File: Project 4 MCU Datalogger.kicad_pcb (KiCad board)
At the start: 2 copper layers, 29 parts, among them J1 Conn_02x03_Odd_Even, J2 Conn_01x04_Pin, J3 Conn_01x09_Pin, J4 Conn_01x04_Pin, U1 24LC1025, U2 24LC1025, U3 DS1337S_, U4 ATMEGA328P-AU, Y1 32.768kHZ, Y2 16MHz

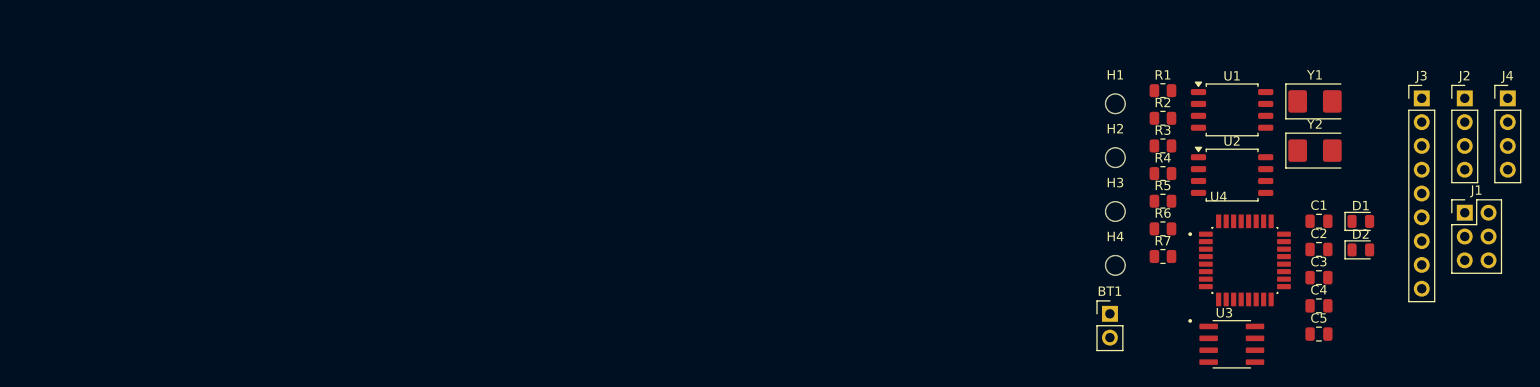
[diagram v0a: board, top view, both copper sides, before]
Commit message: Placed footprints on the Pcbnew.
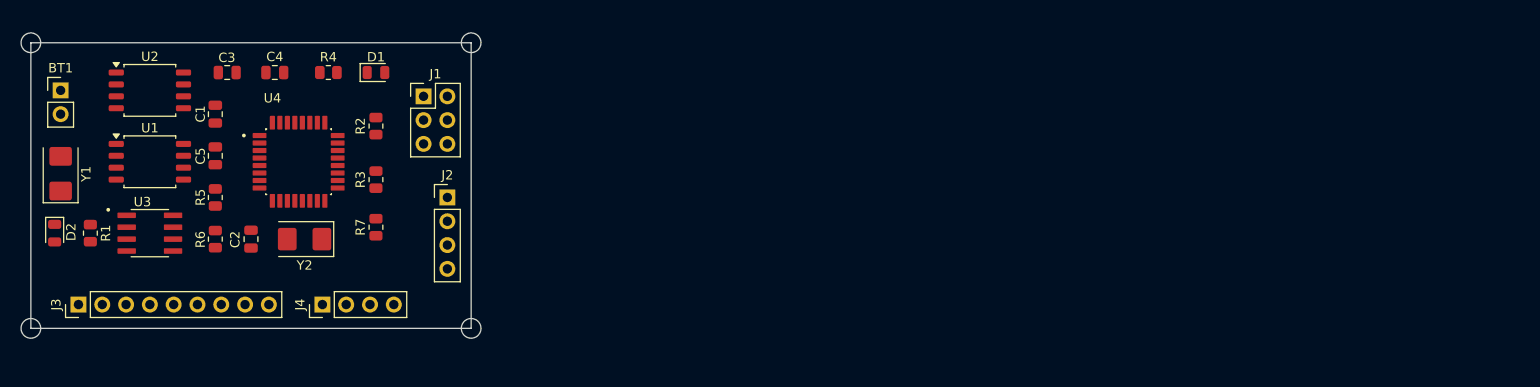
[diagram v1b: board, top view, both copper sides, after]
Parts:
- moved J3 145.0 mm to (106.7, 104.1), turned to 90 degrees
- moved D2 139.4 mm to (104.1, 96.5), turned to -90 degrees
- moved Y1 134.1 mm to (104.8, 90.2), turned to 90 degrees
- moved J4 128.4 mm to (132.7, 104.1), turned to 90 degrees
- moved C5 119.3 mm to (121.3, 88.3), turned to 90 degrees
- moved C3 118.6 mm to (122.6, 79.4), turned to 180 degrees
- moved C1 118.3 mm to (121.3, 83.8), turned to -90 degrees
- moved U3 116.1 mm to (114.3, 96.5)
- moved H4 115.9 mm to (101.6, 106.7)
- moved H1 115.9 mm to (101.6, 76.2)
- moved U2 115.9 mm to (114.3, 81.3)
- moved U1 115.6 mm to (114.3, 88.9)
- moved R1 115.5 mm to (108.0, 96.5), turned to -90 degrees
- moved BT1 114.5 mm to (104.8, 81.3)
- moved C4 114.2 mm to (127.6, 79.4)
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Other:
- board outline added: 47 x 30.5 mm

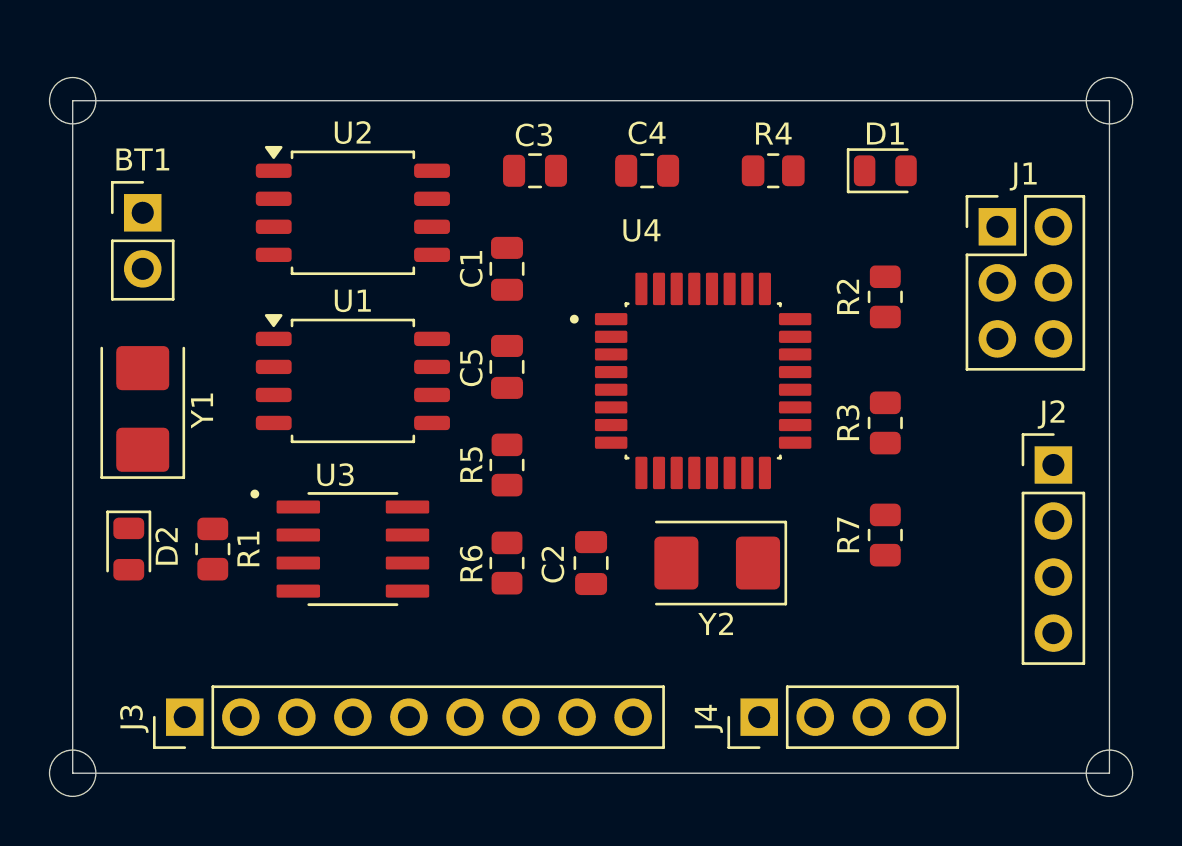
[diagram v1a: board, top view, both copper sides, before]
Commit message: Placed tracks on the Pcbnew.
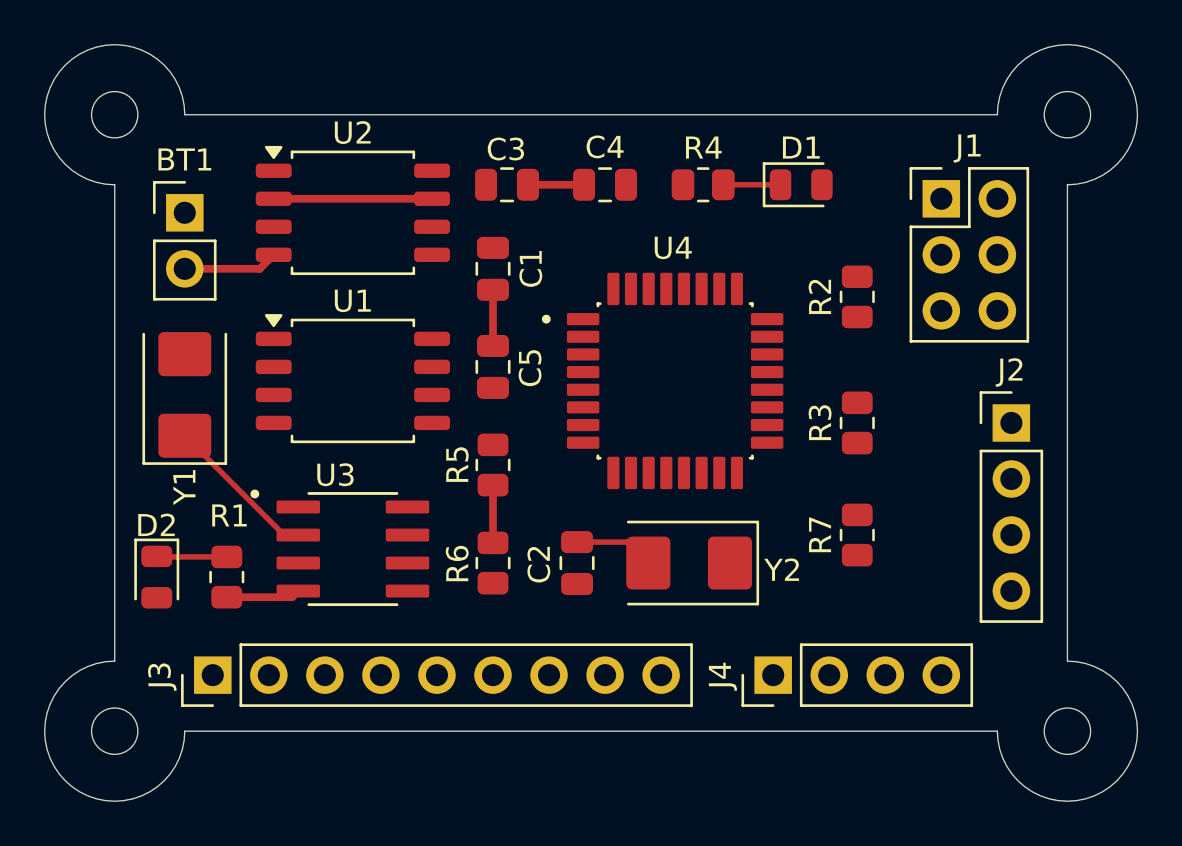
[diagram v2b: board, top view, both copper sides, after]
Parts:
- moved D1 3.86 mm to (134.6, 80.0)
- moved R4 3.24 mm to (130.2, 80.0)
- moved J1 2.84 mm to (141.0, 80.6)
- moved H3 2.69 mm to (146.7, 104.8)
- moved H4 2.69 mm to (103.5, 104.8)
- moved J2 2.69 mm to (144.1, 90.8)
- moved J3 2.29 mm to (108.0, 102.2)
- moved C4 2.01 mm to (125.7, 80.0)
- moved Y1 2.01 mm to (106.7, 89.5)
- moved H1 2.01 mm to (103.5, 76.8)
- moved H2 2.01 mm to (146.7, 76.8)
- moved J4 2.01 mm to (133.3, 102.2)
- moved BT1 1.91 mm to (106.7, 81.3)
- moved D2 1.80 mm to (105.4, 97.8)
- moved C3 1.42 mm to (121.3, 80.0)
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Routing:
- net GND: track 0.00 -> 19.9 mm
- net Net-(U3-X2): track 0.00 -> 7.01 mm
- net Net-(U4-PB6): track 0.00 -> 3.62 mm
- net Net-(D2-K): track 0.00 -> 3.19 mm
- net /Vcc: track 0.00 -> 2.62 mm
- net Net-(D1-K): track 0.00 -> 2.59 mm
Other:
- board size 47 x 30.5 mm -> 49.5 x 34.3 mm

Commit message: Wiring completed.
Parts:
- added REF**: KiCad-Logo2_5mm_SilkScreen, Symbol:KiCad-Logo2_5mm_SilkScreen, B.Cu at (114.3, 97.5)
- moved R2 5.72 mm to (137.2, 90.8)
- moved R3 5.72 mm to (137.2, 85.1)
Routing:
- net /Vcc: track 2.62 -> 142.4 mm, vias 0 -> 23
- net GND: track 19.9 -> 92.7 mm, vias 0 -> 8
- net /SCL: track 0.00 -> 60.7 mm, vias 0 -> 4
- net /SDA: track 0.00 -> 55.4 mm, vias 0 -> 3
- net /MOSI: track 0.00 -> 36.2 mm, vias 0 -> 2
- net /D2: track 0.00 -> 33.9 mm, vias 0 -> 2
- net /TX: track 0.00 -> 30.5 mm, vias 0 -> 2
- net /MISO: track 0.00 -> 28.4 mm, vias 0 -> 2
- net /D3: track 0.00 -> 27.9 mm, vias 0 -> 2
- net Net-(U4-PB7): track 0.00 -> 27.5 mm, vias 0 -> 2
- net /RESET: track 0.00 -> 26.0 mm, vias 0 -> 2
- net /D4: track 0.00 -> 24.6 mm, vias 0 -> 2
- net /RX: track 0.00 -> 22.0 mm, vias 0 -> 2
- net /SCK: track 0.00 -> 20.7 mm
- net Net-(U4-AREF): track 0.00 -> 18.2 mm
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- added copper zone on F.Cu, net /Vcc
- added copper zone on B.Cu, net GND
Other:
- board size 49.5 x 34.3 mm -> 48.5 x 33.3 mm

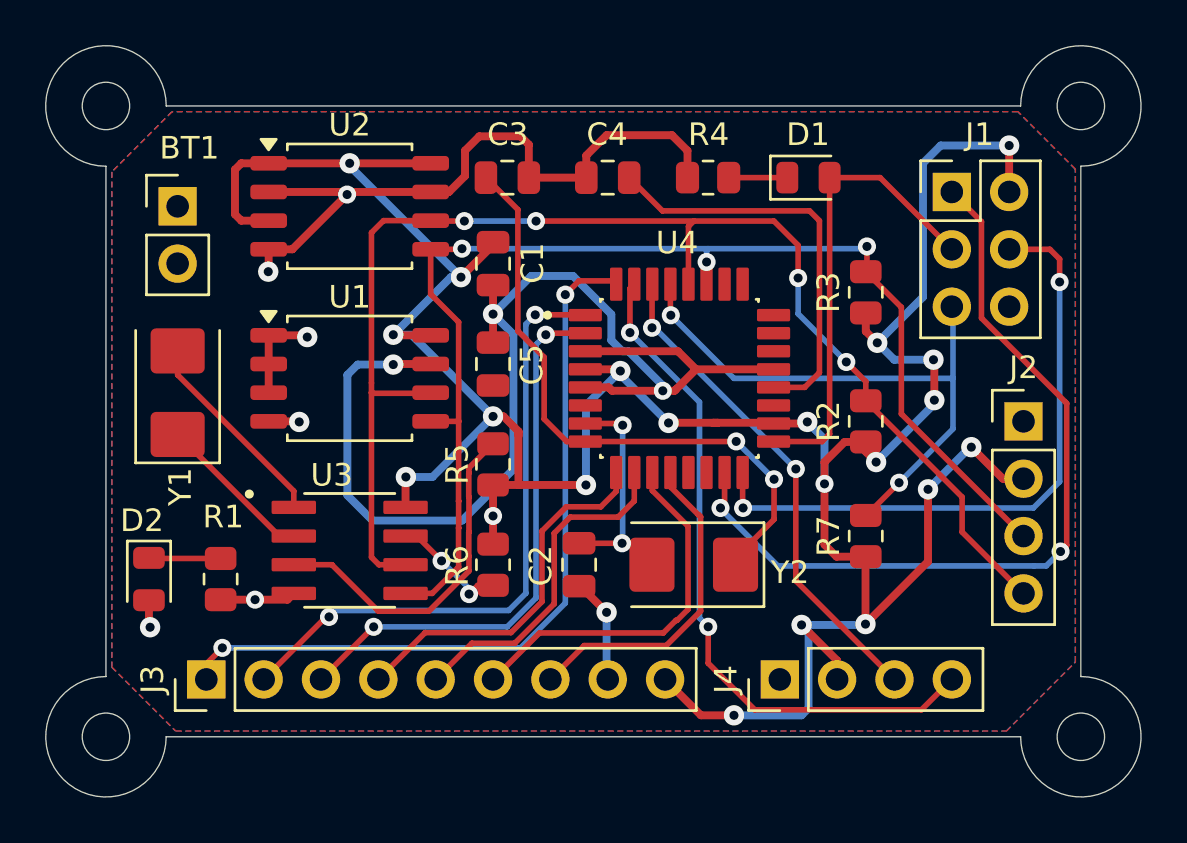
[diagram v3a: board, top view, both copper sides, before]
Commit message: Placed tracks in the Pcbnew.
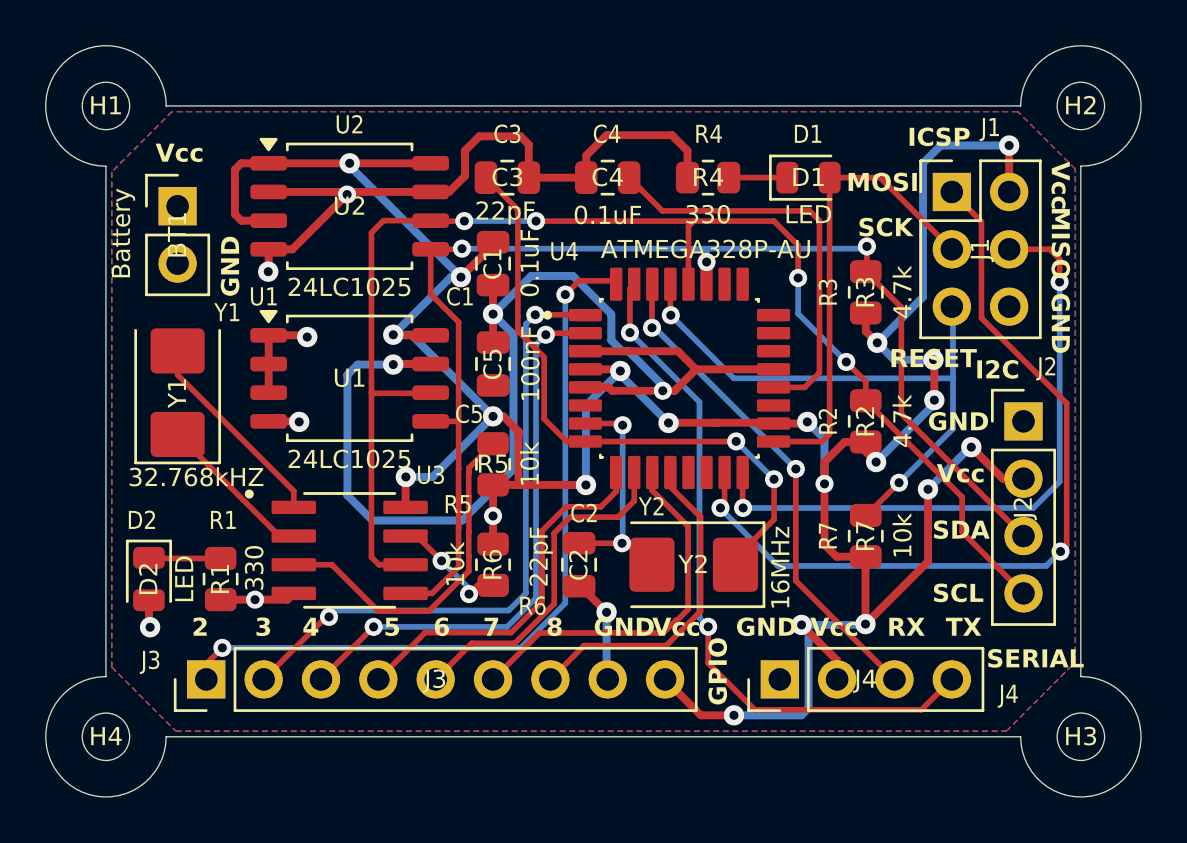
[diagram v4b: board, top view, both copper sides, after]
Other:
- board text added: "- 2Mbit EEPROM - RTC - I2C, SPI, GPIOs"
- board text added: "2"
- board text added: "3"
- board text added: "4"
- board text added: "5"
- board text added: "6"
- board text added: "7"
- board text added: "8"
- board text added: "Data Logger with the ATMega328P."
- board text added: "GND"
- board text added: "GPIO"
- board text added: "I2C"
- board text added: "ICSP"
- board text added: "MISO"
- board text added: "MOSI"
- board text added: "RESET"
- board text added: "RX"
- board text added: "SCK"
- board text added: "SCL"
- board text added: "SDA"
- board text added: "SERIAL"
- board text added: "TX"
- board text added: "Vcc"
